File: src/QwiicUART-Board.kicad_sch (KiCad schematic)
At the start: 14 parts, among them J1 QWIIC, J2 QWIIC, J3 FTDI, U1 SC16IS741A, X1 ECS-2520MVLC-018-BN-TR

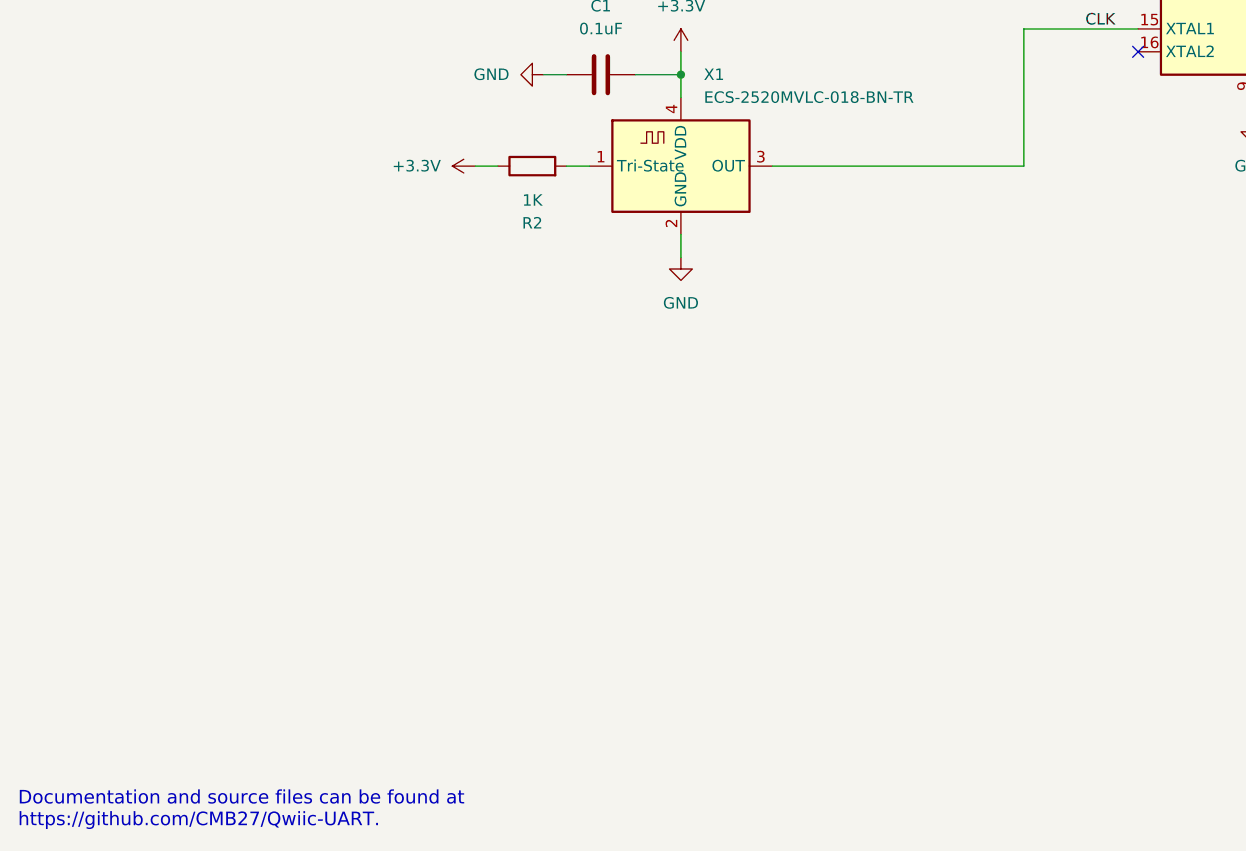
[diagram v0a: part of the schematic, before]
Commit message: Changed repository name. Changed address numbers on back of board. Added a test point for the clock.
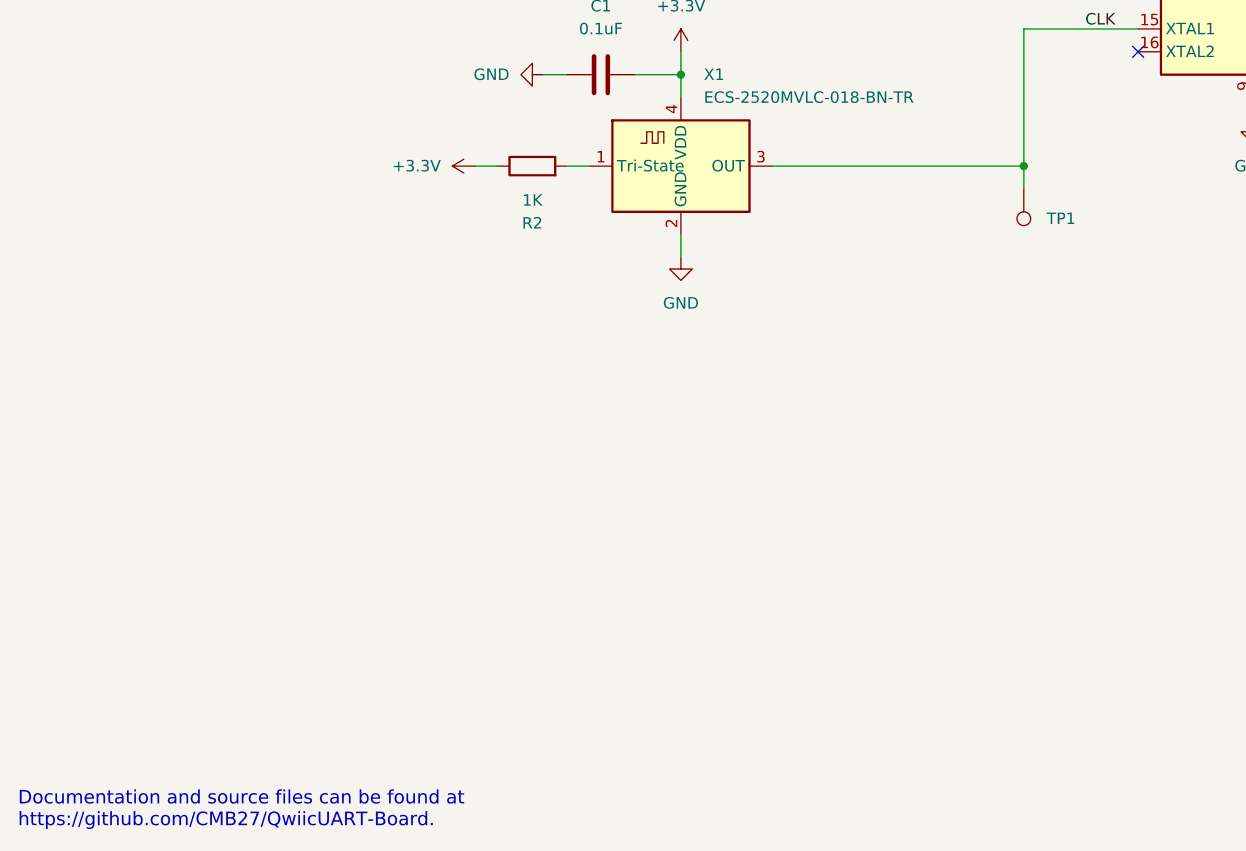
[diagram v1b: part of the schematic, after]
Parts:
- added TP1: TestPoint, TestPoint:TestPoint_THTPad_D1.0mm_Drill0.5mm, symbol Connector:TestPoint
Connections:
- net CLK: now also TP1.1
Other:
- note added: "Documentation and source files can be found at https://github.com/CMB27/QwiicUART-Board."
- note removed: "Documentation and source files can be found at https://github.com/CMB27/Qwiic-UART."
- title: Qwiic UART -> Qwiic UART Board
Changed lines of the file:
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@@
 	(paper "USLetter")
 	(title_block
-		(title "Qwiic UART")
-		(date "2025-01-11")
-		(rev "0.0.1")
+		(title "Qwiic UART Board")
+		(date "2025-02-08")
+		(rev "0.0.2")
 		(company "Designer: C. M. Bulliner")
 		(comment 2 "OF MERCHANTABILITY, SATISFACTORY QUALITY AND FITNESS FOR A PARTICULAR PURPOSE.")
@@
 		(color 0 0 0 0)
 	)
+	(junction
+		(at 127 127)
+		(diameter 0)
+		(color 0 0 0 0)
+	)
 	(no_connect
 		(at 81.28 33.02)
@@
 	(wire
 		(pts
+			(xy 127 127) (xy 127 129.54)
+		)
+		(stroke
+			(width 0)
+			(type default)
+		)
+	)
+	(wire
+		(pts
 			(xy 231.14 114.3) (xy 228.6 114.3)
 		)
@@
 		)
 	)
-	(text "Documentation and source files can be found at\nhttps://github.com/CMB27/Qwiic-UART."
+	(text "Documentation and source files can be found at\nhttps://github.com/CMB27/QwiicUART-Board."
 		(exclude_from_sim no)
 		(at 15.24 200.66 0)
@@
 			)
 			(justify left bottom)
-			(href "https://github.com/CMB27/Qwiic-UART")
+			(href "https://github.com/CMB27/QwiicUART-Board")
 		)
 	)
@@
 					(unit 1)
 				)
+			)
+		)
+	)
+	(symbol
+		(lib_id "Connector:TestPoint")
+		(at 127 129.54 180)
+		(unit 1)
+		(exclude_from_sim no)
+		(in_bom yes)
+		(on_board yes)
+		(dnp no)
+		(fields_autoplaced yes)
+		(property "Reference" "TP1"
+			(at 129.54 132.8419 0)
+			(effects
+				(font
+					(size 1.27 1.27)
+				)
+				(justify right)
+			)
+		)
+		(property "Value" "TestPoint"
+			(at 129.54 134.1119 0)
+			(effects
+				(font
+					(size 1.27 1.27)
+				)
+				(justify right)
+				(hide yes)
+			)
+		)
+		(property "Footprint" "TestPoint:TestPoint_THTPad_D1.0mm_Drill0.5mm"
+			(at 121.92 129.54 0)
+			(effects
+				(font
+					(size 1.27 1.27)
+				)
+				(hide yes)
+			)
+		)
+		(property "Datasheet" "~"
+			(at 121.92 129.54 0)
+			(effects
+				(font
+					(size 1.27 1.27)
+				)
+				(hide yes)
+			)
+		)
+		(property "Description" "test point"
+			(at 127 129.54 0)
+			(effects
+				(font
+					(size 1.27 1.27)
+				)
+				(hide yes)
+			)
+		)
+		(pin "1"
+		)
+		(instances
+			(project ""
+				(path "/0a62f701-930c-47ca-8e1b-6bdebd71a431"
+					(reference "TP1")
+					(unit 1)
+				)
